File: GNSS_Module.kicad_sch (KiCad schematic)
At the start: 18 parts, among them J16 GPS_Transmission_Conn, J2 FTDI_Conn, J4 GPS_Transmission_Conn, U11 ublox_SAM-M8Q

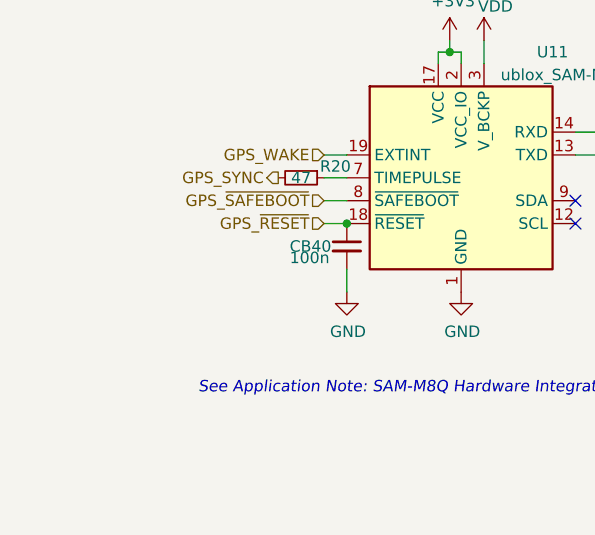
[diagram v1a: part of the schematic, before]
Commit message: (sch) split out GPS NRST
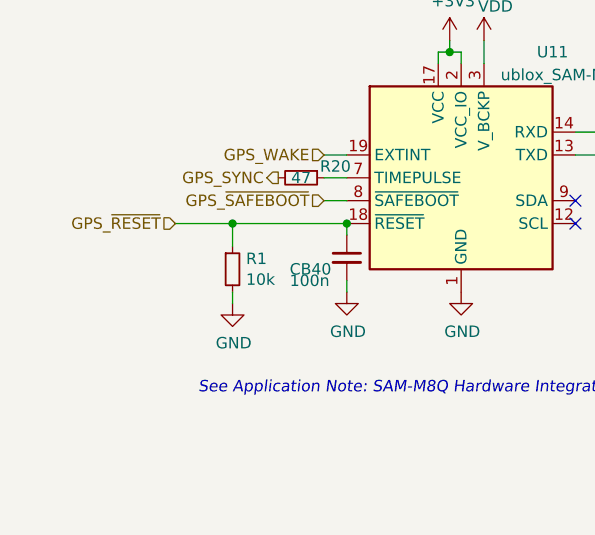
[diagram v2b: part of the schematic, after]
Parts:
- added R1: 10k, Resistor_SMD:R_0603_1608Metric_Pad0.98x0.95mm_HandSolder, symbol Device:R_Small
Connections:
- net GND: now also R1.2
- net GPS_~{RESET}: now also R1.1
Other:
- moved on the sheet: CB40
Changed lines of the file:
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@@
   (junction (at 57.15 31.75) (diameter 0) (color 0 0 0 0)
+  )
+  (junction (at 52.07 100.33) (diameter 0) (color 0 0 0 0)
   )
   (junction (at 194.31 80.01) (diameter 0) (color 0 0 0 0)
@@
     (stroke (width 0) (type default))
   )
+  (wire (pts (xy 52.07 100.33) (xy 52.07 102.87))
+    (stroke (width 0) (type default))
+  )
   (wire (pts (xy 53.34 40.64) (xy 53.34 44.45))
     (stroke (width 0) (type default))
@@
     (stroke (width 0) (type default))
   )
+  (wire (pts (xy 52.07 107.95) (xy 52.07 109.22))
+    (stroke (width 0) (type default))
+  )
   (wire (pts (xy 76.2 81.28) (xy 77.47 81.28))
     (stroke (width 0) (type default))
   )
+  (wire (pts (xy 64.77 101.6) (xy 64.77 100.33))
+    (stroke (width 0) (type default))
+  )
   (wire (pts (xy 190.5 80.01) (xy 190.5 78.74))
     (stroke (width 0) (type default))
@@
     (stroke (width 0) (type default))
   )
-  (wire (pts (xy 64.77 107.95) (xy 64.77 105.41))
+  (wire (pts (xy 64.77 107.95) (xy 64.77 106.68))
     (stroke (width 0) (type default))
   )
@@
     (stroke (width 0) (type default))
   )
+  (wire (pts (xy 52.07 100.33) (xy 64.77 100.33))
+    (stroke (width 0) (type default))
+  )
   (polyline (pts (xy 124.46 21.59) (xy 40.64 21.59))
     (stroke (width 0) (type default))
@@
     (stroke (width 0) (type default))
   )
-  (wire (pts (xy 62.23 100.33) (xy 64.77 100.33))
+  (wire (pts (xy 45.72 100.33) (xy 52.07 100.33))
     (stroke (width 0) (type default))
   )
@@
     (effects (font (size 1.27 1.27)) (justify right))
   )
-  (hierarchical_label "GPS_~{RESET}" (shape input) (at 62.23 100.33 180) (fields_autoplaced)
+  (hierarchical_label "GPS_~{RESET}" (shape input) (at 45.72 100.33 180) (fields_autoplaced)
     (effects (font (size 1.27 1.27)) (justify right))
   )
@@
     )
   )
-  (symbol (lib_id "Device:C_Small") (at 64.77 102.87 0) (unit 1)
-    (in_bom yes) (on_board yes) (dnp no)
-    (property "Reference" "CB40" (at 58.42 102.87 0)
-      (effects (font (size 1.27 1.27)) (justify left))
-    )
-    (property "Value" "100n" (at 58.42 104.14 0)
-      (effects (font (size 1.27 1.27)) (justify left))
-    )
-    (property "Footprint" "Capacitor_SMD:C_0603_1608Metric_Pad1.08x0.95mm_HandSolder" (at 64.77 102.87 0)
-      (effects (font (size 1.27 1.27)) hide)
-    )
-    (property "Datasheet" "~" (at 64.77 102.87 0)
-      (effects (font (size 1.27 1.27)) hide)
-    )
-    (property "MPN" "C0603C104M5RACTU" (at 64.77 102.87 0)
-      (effects (font (size 1.27 1.27)) hide)
-    )
-    (property "Mfr." "KEMET" (at 64.77 102.87 0)
+  (symbol (lib_id "Device:C_Small") (at 64.77 104.14 0) (unit 1)
+    (in_bom yes) (on_board yes) (dnp no)
+    (property "Reference" "CB40" (at 58.42 105.41 0)
+      (effects (font (size 1.27 1.27)) (justify left))
+    )
+    (property "Value" "100n" (at 58.42 106.68 0)
+      (effects (font (size 1.27 1.27)) (justify left))
+    )
+    (property "Footprint" "Capacitor_SMD:C_0603_1608Metric_Pad1.08x0.95mm_HandSolder" (at 64.77 104.14 0)
+      (effects (font (size 1.27 1.27)) hide)
+    )
+    (property "Datasheet" "~" (at 64.77 104.14 0)
+      (effects (font (size 1.27 1.27)) hide)
+    )
+    (property "MPN" "C0603C104M5RACTU" (at 64.77 104.14 0)
+      (effects (font (size 1.27 1.27)) hide)
+    )
+    (property "Mfr." "KEMET" (at 64.77 104.14 0)
       (effects (font (size 1.27 1.27)) hide)
     )
@@
         )
       )
+    )
+  )
+  (symbol (lib_id "power:GND") (at 52.07 109.22 0) (unit 1)
+    (in_bom yes) (on_board yes) (dnp no)
+    (property "Reference" "#PWR078" (at 52.07 115.57 0)
+      (effects (font (size 1.27 1.27)) hide)
+    )
+    (property "Value" "GND" (at 52.197 113.6142 0)
+      (effects (font (size 1.27 1.27)))
+    )
+    (property "Footprint" "" (at 52.07 109.22 0)
+      (effects (font (size 1.27 1.27)) hide)
+    )
+    (property "Datasheet" "" (at 52.07 109.22 0)
+      (effects (font (size 1.27 1.27)) hide)
+    )
+    (pin "1")
+    (instances
+      (project "kleinvoet"
+        (path "/4185c36c-c66e-4dbd-be5d-841e551f4885/00000000-0000-0000-0000-00005edf3693"
+          (reference "#PWR078") (unit 1)
+        )
+      )
+    )
+  )
+  (symbol (lib_id "Device:R_Small") (at 52.07 105.41 0) (unit 1)
+    (in_bom yes) (on_board yes) (dnp no)
+    (property "Reference" "R1" (at 53.5686 104.2416 0)
+      (effects (font (size 1.27 1.27)) (justify left))
+    )
+    (property "Value" "10k" (at 53.5686 106.553 0)
+      (effects (font (size 1.27 1.27)) (justify left))
+    )
+    (property "Footprint" "Resistor_SMD:R_0603_1608Metric_Pad0.98x0.95mm_HandSolder" (at 52.07 105.41 0)
+      (effects (font (size 1.27 1.27)) hide)
+    )
+    (property "Datasheet" "~" (at 52.07 105.41 0)
+      (effects (font (size 1.27 1.27)) hide)
+    )
+    (property "MPN" "RC0603JR-0710KL" (at 52.07 105.41 0)
+      (effects (font (size 1.27 1.27)) hide)
+    )
+    (property "Mfr." "Yageo" (at 52.07 105.41 0)
+      (effects (font (size 1.27 1.27)) hide)
+    )
+    (pin "1")
+    (pin "2")
+    (instances
+      (project "kleinvoet"
+        (path "/4185c36c-c66e-4dbd-be5d-841e551f4885"
+          (reference "R1") (unit 1)
+        )
+        (path "/4185c36c-c66e-4dbd-be5d-841e551f4885/00000000-0000-0000-0000-00005edf3693"
+          (reference "R35") (unit 1)
+        )
+      )

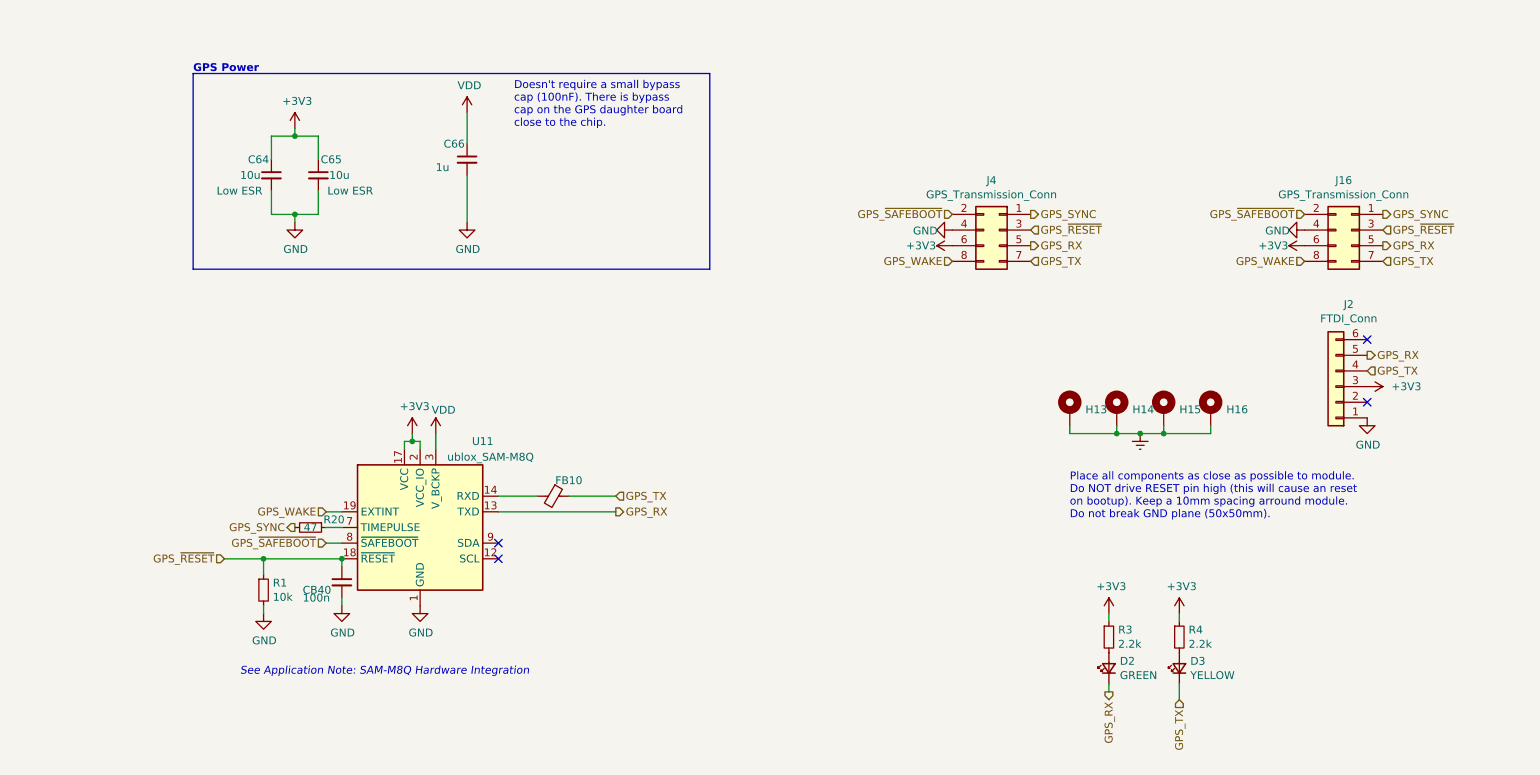
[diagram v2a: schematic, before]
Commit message: (sch) add timepulse LED
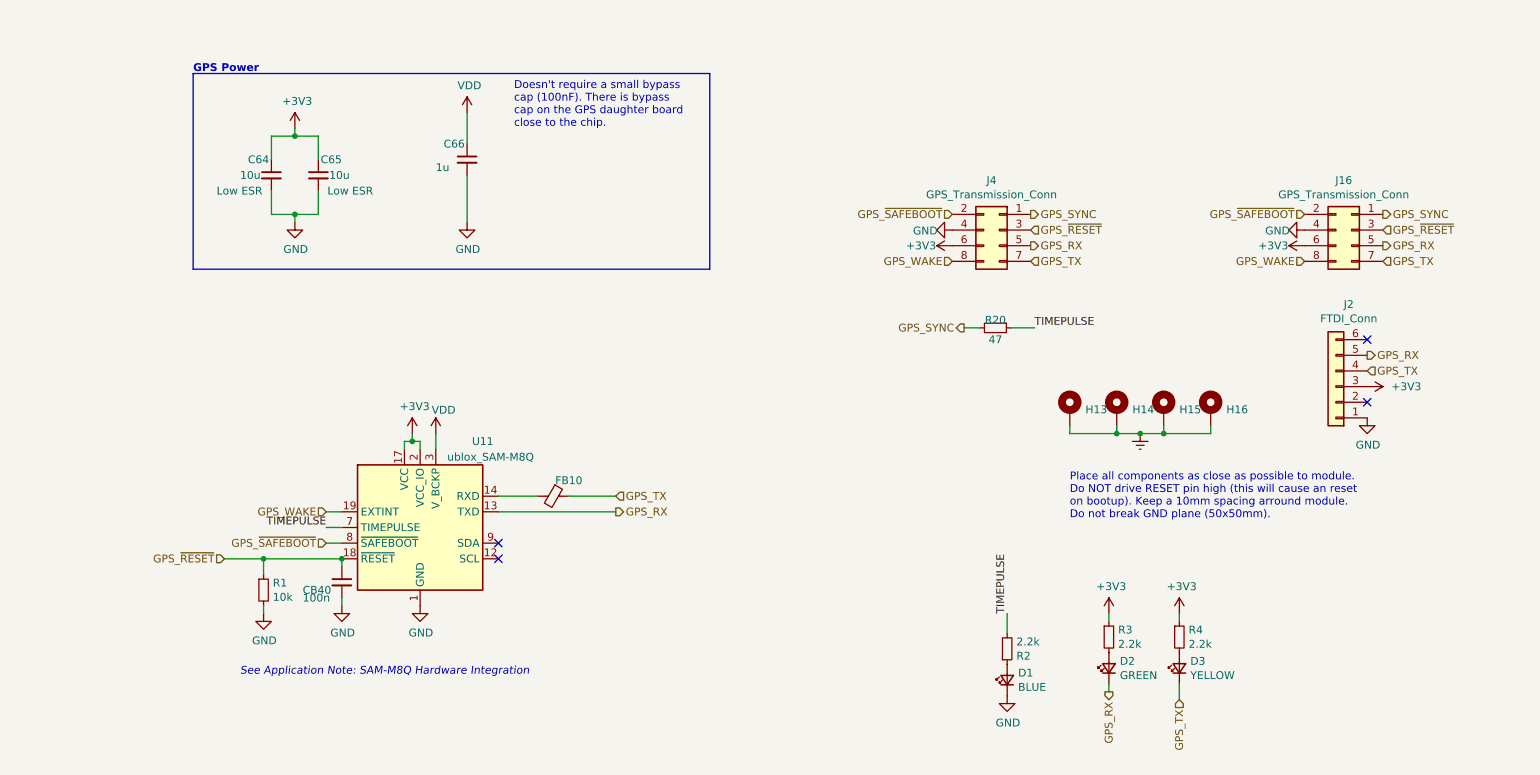
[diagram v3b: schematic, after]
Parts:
- added D1: BLUE, LED_SMD:LED_0603_1608Metric_Pad1.05x0.95mm_HandSolder, symbol Device:LED_Small
- added R2: 2.2k, Resistor_SMD:R_0603_1608Metric_Pad0.98x0.95mm_HandSolder, symbol Device:R_Small
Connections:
- net GND: now also D1.1 (K)
- net TIMEPULSE: now reaches R20.1, U11.7 (TIMEPULSE)
- net TIMEPULSE: now also R2.2
- new net: D1.2 (A), R2.1
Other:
- moved on the sheet: R20
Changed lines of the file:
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@@
+    (stroke (width 0) (type default))
+  )
+  (wire (pts (xy 165.735 62.865) (xy 168.275 62.865))
+    (stroke (width 0) (type default))
+  )
+  (wire (pts (xy 172.72 109.22) (xy 172.72 112.395))
     (stroke (width 0) (type default))
   )
@@
   )
   (wire (pts (xy 182.88 80.01) (xy 182.88 78.74))
+    (stroke (width 0) (type default))
+  )
+  (wire (pts (xy 173.355 62.865) (xy 177.165 62.865))
     (stroke (width 0) (type default))
   )
@@
     (effects (font (size 1.27 1.27)) (justify left bottom))
   )
+  (label "TIMEPULSE" (at 62.23 95.25 180) (fields_autoplaced)
+    (effects (font (size 1.27 1.27)) (justify right bottom))
+  )
+  (label "TIMEPULSE" (at 177.165 62.865 0) (fields_autoplaced)
+    (effects (font (size 1.27 1.27)) (justify left bottom))
+  )
+  (label "TIMEPULSE" (at 172.72 109.22 90) (fields_autoplaced)
+    (effects (font (size 1.27 1.27)) (justify left bottom))
+  )
   (hierarchical_label "GPS_~{SAFEBOOT}" (shape input) (at 62.23 97.79 180) (fields_autoplaced)
     (effects (font (size 1.27 1.27)) (justify right))
@@
     (effects (font (size 1.27 1.27)) (justify left))
   )
-  (hierarchical_label "GPS_SYNC" (shape output) (at 57.15 95.25 180) (fields_autoplaced)
+  (hierarchical_label "GPS_SYNC" (shape output) (at 165.735 62.865 180) (fields_autoplaced)
     (effects (font (size 1.27 1.27)) (justify right))
   )
@@
       (effects (font (size 1.27 1.27)) hide)
     )
-    (property "MFN" "" (at 189.23 113.03 0)
-      (effects (font (size 1.27 1.27)) hide)
-    )
     (property "Mfr." "Yageo" (at 189.23 113.03 0)
       (effects (font (size 1.27 1.27)) hide)
@@
     )
     (property "Datasheet" "~" (at 189.23 118.11 90)
-      (effects (font (size 1.27 1.27)) hide)
-    )
-    (property " MPN" "" (at 189.23 118.11 90)
       (effects (font (size 1.27 1.27)) hide)
     )
@@
     )
   )
-  (symbol (lib_id "Device:R_Small") (at 59.69 95.25 270) (unit 1)
-    (in_bom yes) (on_board yes) (dnp no)
-    (property "Reference" "R20" (at 63.5 93.98 90)
-      (effects (font (size 1.27 1.27)))
-    )
-    (property "Value" "47" (at 59.69 95.25 90)
-      (effects (font (size 1.27 1.27)))
-    )
-    (property "Footprint" "Resistor_SMD:R_0603_1608Metric_Pad0.98x0.95mm_HandSolder" (at 59.69 95.25 0)
-      (effects (font (size 1.27 1.27)) hide)
-    )
-    (property "Datasheet" "~" (at 59.69 95.25 0)
-      (effects (font (size 1.27 1.27)) hide)
-    )
-    (property "MPN" "ERJ-3EKF47R0V" (at 59.69 95.25 0)
-      (effects (font (size 1.27 1.27)) hide)
-    )
-    (property "Mfr." "Panasonic" (at 59.69 95.25 0)
+  (symbol (lib_id "Device:R_Small") (at 170.815 62.865 270) (unit 1)
+    (in_bom yes) (on_board yes) (dnp no)
+    (property "Reference" "R20" (at 170.815 61.595 90)
+      (effects (font (size 1.27 1.27)))
+    )
+    (property "Value" "47" (at 170.815 64.77 90)
+      (effects (font (size 1.27 1.27)))
+    )
+    (property "Footprint" "Resistor_SMD:R_0603_1608Metric_Pad0.98x0.95mm_HandSolder" (at 170.815 62.865 0)
+      (effects (font (size 1.27 1.27)) hide)
+    )
+    (property "Datasheet" "~" (at 170.815 62.865 0)
+      (effects (font (size 1.27 1.27)) hide)
+    )
+    (property "MPN" "ERJ-3EKF47R0V" (at 170.815 62.865 0)
+      (effects (font (size 1.27 1.27)) hide)
+    )
+    (property "Mfr." "Panasonic" (at 170.815 62.865 0)
       (effects (font (size 1.27 1.27)) hide)
     )
@@
     )
   )
+  (symbol (lib_id "Device:R_Small") (at 172.72 114.935 0) (mirror x) (unit 1)
+    (in_bom yes) (on_board yes) (dnp no)
+    (property "Reference" "R2" (at 174.2186 116.1034 0)
+      (effects (font (size 1.27 1.27)) (justify left))
+    )
+    (property "Value" "2.2k" (at 174.2186 113.792 0)
+      (effects (font (size 1.27 1.27)) (justify left))
+    )
+    (property "Footprint" "Resistor_SMD:R_0603_1608Metric_Pad0.98x0.95mm_HandSolder" (at 172.72 114.935 0)
+      (effects (font (size 1.27 1.27)) hide)
+    )
+    (property "Datasheet" "~" (at 172.72 114.935 0)
+      (effects (font (size 1.27 1.27)) hide)
+    )
+    (property "MPN" "RC0603FR-072K2L" (at 172.72 114.935 0)
+      (effects (font (size 1.27 1.27)) hide)
+    )
+    (property "Mfr." "Yageo" (at 172.72 114.935 0)
+      (effects (font (size 1.27 1.27)) hide)
+    )
+    (pin "1")
+    (pin "2")
+    (instances
+      (project "kleinvoet"
+        (path "/4185c36c-c66e-4dbd-be5d-841e551f4885"
+          (reference "R2") (unit 1)
+        )
+        (path "/4185c36c-c66e-4dbd-be5d-841e551f4885/00000000-0000-0000-0000-00005edf3693"
+          (reference "R55") (unit 1)
+        )
+      )
+    )
+  )
   (symbol (lib_id "Device:R_Small") (at 52.07 105.41 0) (unit 1)
     (in_bom yes) (on_board yes) (dnp no)
@@
         )
       )
+    )
+  )
+  (symbol (lib_id "Device:LED_Small") (at 172.72 120.015 90) (unit 1)
+    (in_bom yes) (on_board yes) (dnp no)
+    (property "Reference" "D1" (at 174.498 118.8466 90)
+      (effects (font (size 1.27 1.27)) (justify right))
+    )
+    (property "Value" "BLUE" (at 174.498 121.158 90)
+      (effects (font (size 1.27 1.27)) (justify right))
+    )
+    (property "Footprint" "LED_SMD:LED_0603_1608Metric_Pad1.05x0.95mm_HandSolder" (at 172.72 120.015 90)
+      (effects (font (size 1.27 1.27)) hide)
+    )
+    (property "Datasheet" "~" (at 172.72 120.015 90)
+      (effects (font (size 1.27 1.27)) hide)
+    )
+    (property "MPN" "SMLD12BN1WT86" (at 172.72 120.015 90)
+      (effects (font (size 1.27 1.27)) hide)
+    )
+    (property "Mfr." "ROHM Semiconductor" (at 172.72 120.015 90)
+      (effects (font (size 1.27 1.27)) hide)
+    )
+    (pin "1")
+    (pin "2")
+    (instances
+      (project "kleinvoet"
+        (path "/4185c36c-c66e-4dbd-be5d-841e551f4885"
+          (reference "D1") (unit 1)
+        )
+        (path "/4185c36c-c66e-4dbd-be5d-841e551f4885/00000000-0000-0000-0000-00005edf3693"
+          (reference "D5") (unit 1)
+        )
+      )
+    )
+  )
+  (symbol (lib_id "power:GND") (at 172.72 122.555 0) (unit 1)
+    (in_bom yes) (on_board yes) (dnp no)
+    (property "Reference" "#PWR017" (at 172.72 128.905 0)
+      (effects (font (size 1.27 1.27)) hide)
+    )
+    (property "Value" "GND" (at 172.847 126.9492 0)
+      (effects (font (size 1.27 1.27)))
+    )
+    (property "Footprint" "" (at 172.72 122.555 0)
+      (effects (font (size 1.27 1.27)) hide)
+    )
+    (property "Datasheet" "" (at 172.72 122.555 0)
+      (effects (font (size 1.27 1.27)) hide)
+    )
+    (pin "1")
+    (instances
+      (project "kleinvoet"
+        (path "/4185c36c-c66e-4dbd-be5d-841e551f4885"
+          (reference "#PWR017") (unit 1)
+        )
+        (path "/4185c36c-c66e-4dbd-be5d-841e551f4885/00000000-0000-0000-0000-00005edf3693"
+          (reference "#PWR094") (unit 1)
+        )
+      )

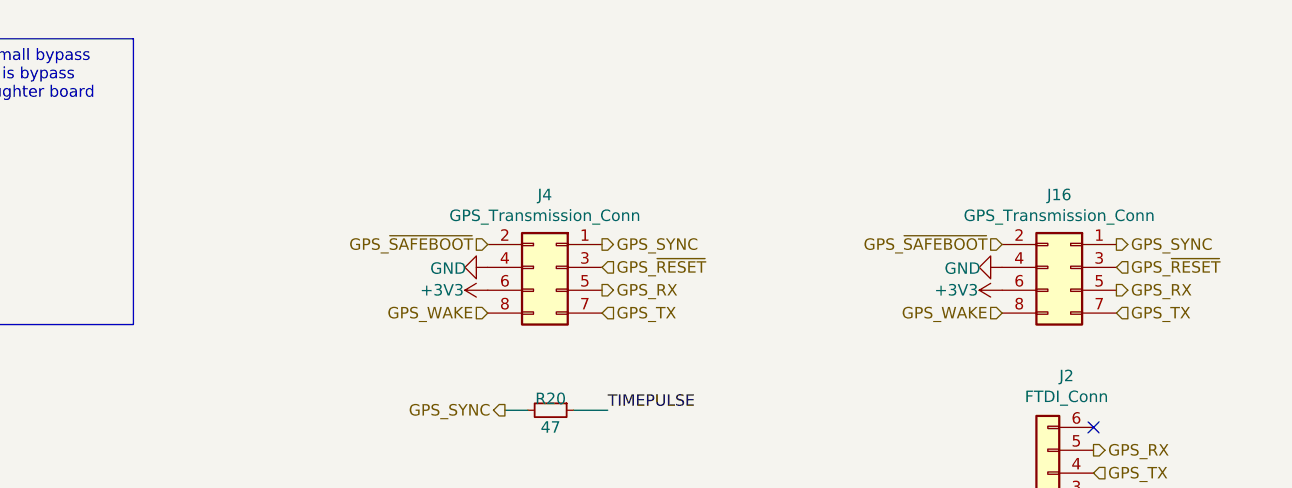
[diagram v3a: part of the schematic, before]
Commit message: (sch) add new GNSS connector
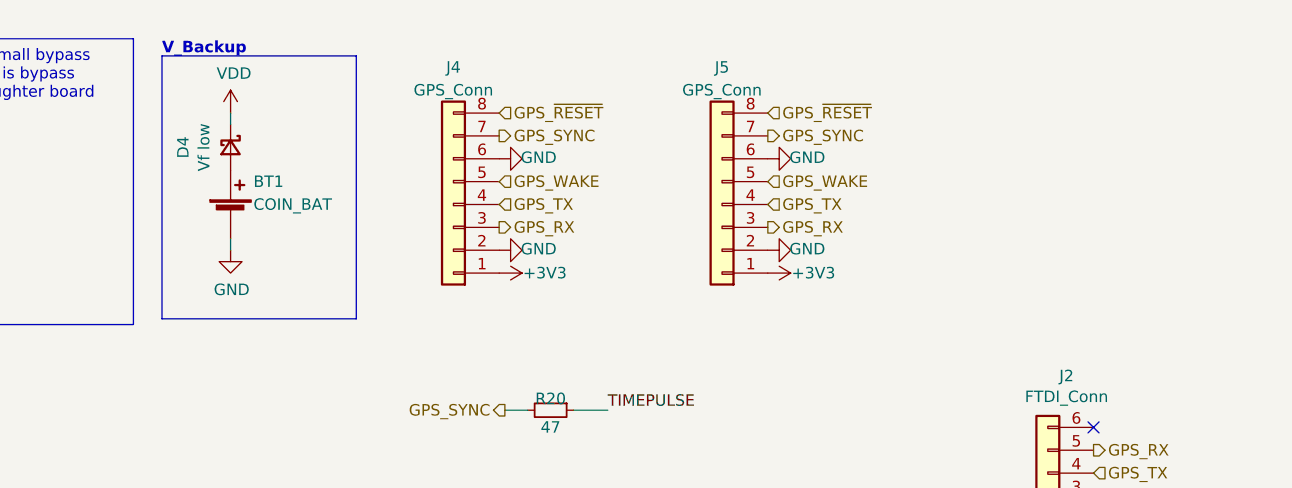
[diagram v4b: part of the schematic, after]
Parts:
- removed J16, J4: GPS_Transmission_Conn, Connector_PinHeader_1.27mm:PinHeader_2x04_P1.27mm_Vertical, symbol Connector_Generic:Conn_02x04_Odd_Even
- added BT1: COIN_BAT, grootvoet:BatteryHolder_Keystone_3002_1x2032, symbol Device:Battery_Cell
- added D4: Vf low, Diode_SMD:D_SOD-123, symbol Device:D_Schottky_Small
- added J4, J5: GPS_Conn, grootvoet:Connector_Amphenol_10114828-xxx08LF_Vertical, symbol Connector_Generic:Conn_01x08
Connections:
- net +3V3: now also J4.1 (Pin_1), J5.1 (Pin_1)
- net GND: now also BT1.2 (-), J4.2 (Pin_2), J4.6 (Pin_6), J5.2 (Pin_2), J5.6 (Pin_6)
- net GPS_RX: now also J4.3 (Pin_3), J5.3 (Pin_3)
- net GPS_SYNC: now also J4.7 (Pin_7), J5.7 (Pin_7)
- net GPS_TX: now also J4.4 (Pin_4), J5.4 (Pin_4)
- net GPS_WAKE: now also J4.5 (Pin_5), J5.5 (Pin_5)
- net GPS_~{RESET}: now also J4.8 (Pin_8), J5.8 (Pin_8)
- net VDD: now also D4.1 (K)
- new net: BT1.1 (+), D4.2 (A)
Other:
- note added: "V_Backup"
